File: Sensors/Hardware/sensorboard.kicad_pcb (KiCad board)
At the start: 4 copper layers, 100 x 50 mm, 260 parts, among them J1 RBUS, J10 1053131104, J11 1053131104, J12 1053131104, J13 1053131104, J14 1053131104, J15 USB_C_Receptacle_USB2.0, J16 Micro_SD_Card_Det, J2 Conn_Coaxial, J3 1053131104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

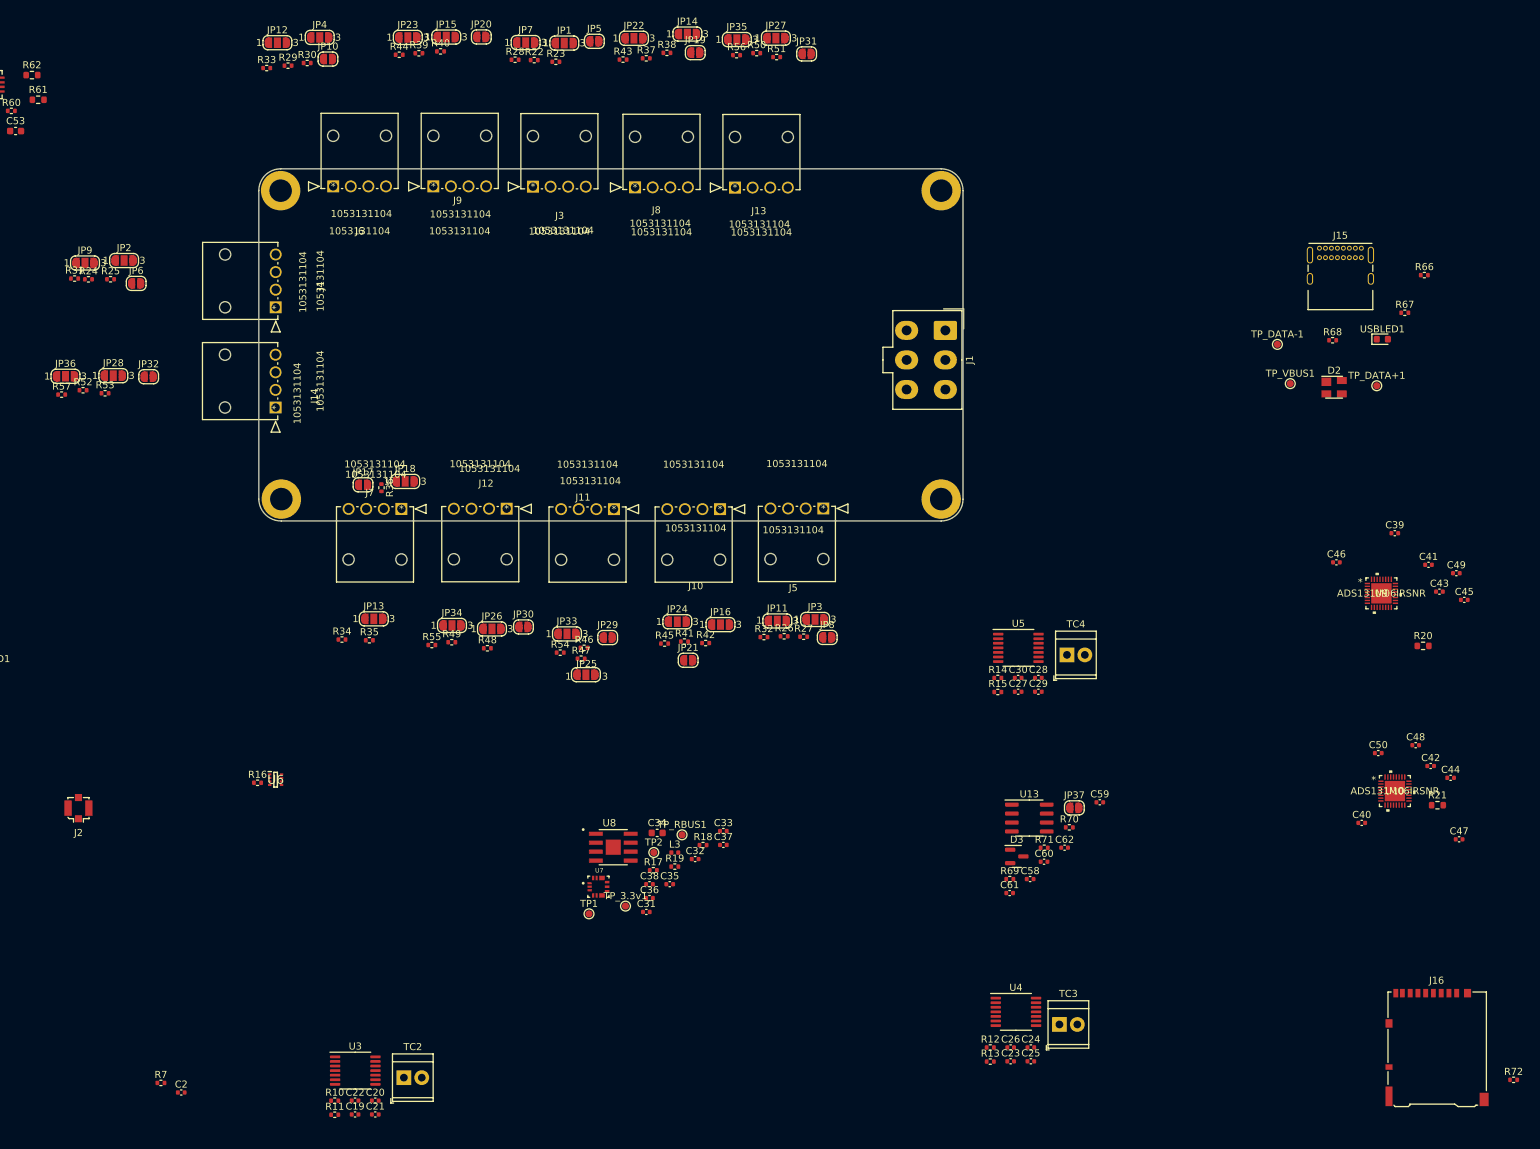
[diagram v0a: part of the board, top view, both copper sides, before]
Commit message: nanofit placements
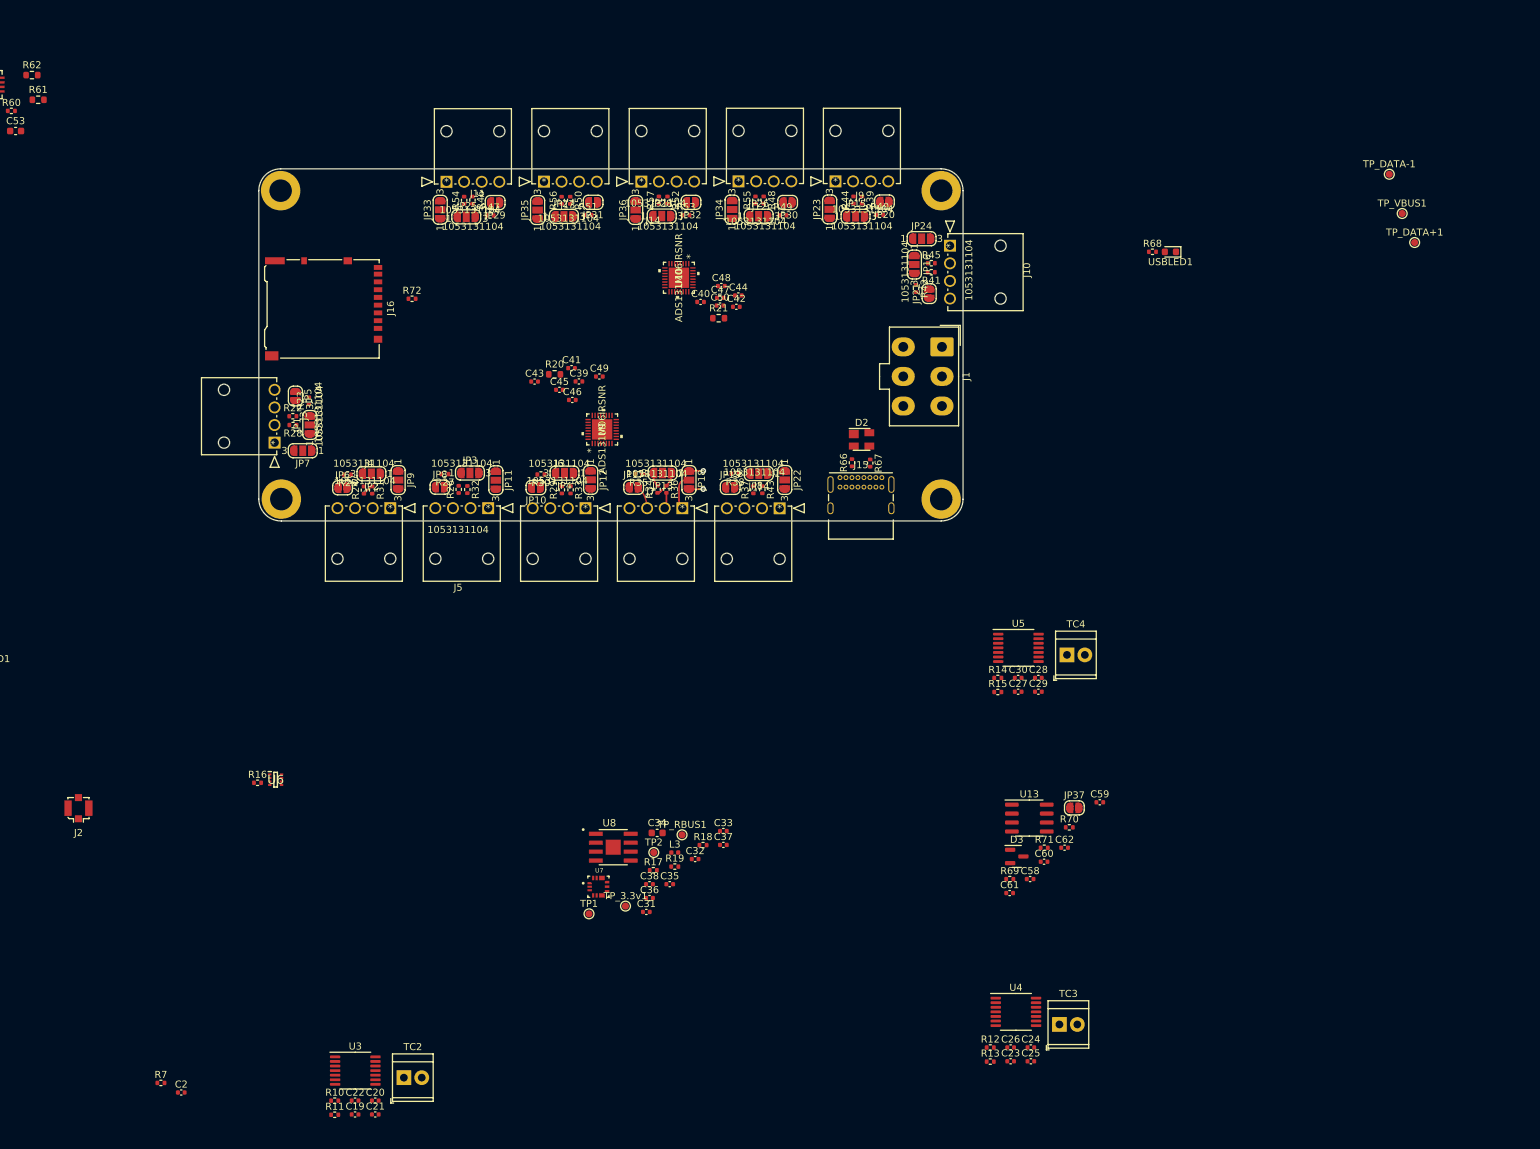
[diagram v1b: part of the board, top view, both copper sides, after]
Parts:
- moved R72 191.8 mm to (121.8, 48.5)
- moved J16 189.7 mm to (109.2, 49.9), turned to -90 degrees
- moved C45 131.9 mm to (142.7, 61.4)
- moved C43 131.9 mm to (139.2, 60.2)
- moved C47 130.1 mm to (165.5, 48.3)
- moved R20 129.2 mm to (142.0, 59.2)
- moved U10 125.1 mm to (159.7, 45.5), turned to -90 degrees
- moved C41 124.9 mm to (144.4, 58.3)
- moved C49 124.9 mm to (148.4, 59.5)
- moved R21 123.3 mm to (165.3, 51.2)
- moved C44 122.2 mm to (168.1, 48.0)
- moved C40 119.5 mm to (162.7, 48.9)
- moved C42 118.2 mm to (167.8, 49.6)
- moved C48 118.2 mm to (165.7, 46.6)
- moved C39 117.8 mm to (145.5, 60.2)
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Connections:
- 12VLED1 pad 1: +3V3 -> GND
- 3V3LED1 pad 1: +3V3 -> GND
- BOOTJUMPER1 pad 2: +3V3 -> GND
- C1 pad 2: +3V3 -> GND
- C10 pad 2: +3V3 -> GND
- C12 pad 2: +3V3 -> GND
- C13 pad 2: +3V3 -> GND
- C14 pad 2: +3V3 -> GND
- C15 pad 1: +3V3 -> GND
- C17 pad 2: +3V3 -> GND
- C18 pad 1: +3V3 -> GND
- C19 pad 1: +3V3 -> GND
- C2 pad 2: +3V3 -> GND
- C21 pad 2: +3V3 -> GND
- C22 pad 1: +3V3 -> GND
- C23 pad 1: +3V3 -> GND
- C25 pad 2: +3V3 -> GND
- C26 pad 1: +3V3 -> GND
- C27 pad 1: +3V3 -> GND
- C29 pad 2: +3V3 -> GND
- C3 pad 2: +3V3 -> GND
- C30 pad 1: +3V3 -> GND
- C31 pad 2: +3V3 -> GND
- C32 pad 2: +3V3 -> GND
- C33 pad 2: +3V3 -> GND
- C34 pad 2: +3V3 -> GND
- C35 pad 2: +3V3 -> GND
- C36 pad 2: +3V3 -> GND
- C37 pad 1: +3V3 -> GND
- C38 pad 1: +3V3 -> GND
- C39 pad 1: +3V3 -> GND
- C4 pad 2: +3V3 -> GND
- C40 pad 1: +3V3 -> GND
- C41 pad 2: +3V3 -> GND
- C42 pad 2: +3V3 -> GND
- C43 pad 2: +3V3 -> GND
- C44 pad 2: +3V3 -> GND
- C45 pad 2: +3V3 -> GND
- C46 pad 2: +3V3 -> GND
- C47 pad 2: +3V3 -> GND
- C48 pad 2: +3V3 -> GND
- C49 pad 2: +3V3 -> GND
- C5 pad 2: +3V3 -> GND
- C50 pad 2: +3V3 -> GND
- C51 pad 2: +3V3 -> GND
- C52 pad 2: +3V3 -> GND
- C53 pad 2: +3V3 -> GND
- C54 pad 2: +3V3 -> GND
- C56 pad 2: +3V3 -> GND
- C57 pad 2: +3V3 -> GND
- C58 pad 2: +3V3 -> GND
- C59 pad 2: +3V3 -> GND
- C6 pad 2: +3V3 -> GND
- C60 pad 2: +3V3 -> GND
- C61 pad 1: +3V3 -> GND
- C62 pad 1: +3V3 -> GND
- C7 pad 2: +3V3 -> GND
- C8 pad 2: +3V3 -> GND
- C9 pad 2: +3V3 -> GND
- D2 pad 1: +3V3 -> GND
- D3 pad 3: +3V3 -> GND
- ENJUMPER1 pad 2: +3V3 -> GND
- H1 pad 1: +3V3 -> GND
- H2 pad 1: +3V3 -> GND
- H3 pad 1: +3V3 -> GND
- H4 pad 1: +3V3 -> GND
- J1 pad 1: +3V3 -> GND
- J1 pad 2: +3V3 -> GND
- J10 pad 4: +3V3 -> GND
- J11 pad 4: +3V3 -> GND
- J12 pad 4: +3V3 -> GND
- J13 pad 4: +3V3 -> GND
- J14 pad 4: +3V3 -> GND
- J15 pad A1: +3V3 -> GND
- J15 pad A12: +3V3 -> GND
- J15 pad B1: +3V3 -> GND
- J15 pad B12: +3V3 -> GND
- J15 pad S1: +3V3 -> GND
- J16 pad 11: +3V3 -> GND
- J16 pad 6: +3V3 -> GND
- J16 pad 9: +3V3 -> GND
- J2 pad 2: +3V3 -> GND
- J3 pad 4: +3V3 -> GND
- J4 pad 4: +3V3 -> GND
- J5 pad 4: +3V3 -> GND
- J6 pad 4: +3V3 -> GND
- J7 pad 4: +3V3 -> GND
- J8 pad 4: +3V3 -> GND
- J9 pad 4: +3V3 -> GND
- JP10 pad 1: +3V3 -> GND
- JP17 pad 1: +3V3 -> GND
- JP19 pad 1: +3V3 -> GND
- JP20 pad 1: +3V3 -> GND
- JP21 pad 1: +3V3 -> GND
- JP29 pad 1: +3V3 -> GND
- JP30 pad 1: +3V3 -> GND
- JP31 pad 1: +3V3 -> GND
- JP32 pad 1: +3V3 -> GND
- JP5 pad 1: +3V3 -> GND
- JP6 pad 1: +3V3 -> GND
- JP8 pad 1: +3V3 -> GND
- R17 pad 2: +3V3 -> GND
- R19 pad 2: +3V3 -> GND
- R23 pad 2: +3V3 -> GND
- R25 pad 2: +3V3 -> GND
- R27 pad 2: +3V3 -> GND
- R30 pad 2: +3V3 -> GND
- R35 pad 2: +3V3 -> GND
- R38 pad 2: +3V3 -> GND
- R4 pad 1: +3V3 -> GND
- R40 pad 2: +3V3 -> GND
- R42 pad 2: +3V3 -> GND
- R47 pad 2: +3V3 -> GND
- R49 pad 2: +3V3 -> GND
- R51 pad 2: +3V3 -> GND
- R53 pad 2: +3V3 -> GND
- R59 pad 2: +3V3 -> GND
- R60 pad 2: +3V3 -> GND
- R64 pad 2: +3V3 -> GND
- R66 pad 2: +3V3 -> GND
- R67 pad 1: +3V3 -> GND
- R69 pad 2: +3V3 -> GND
- U1 pad 57: +3V3 -> GND
- U10 pad 13: +3V3 -> GND
- U10 pad 22: +3V3 -> GND
- U10 pad 28: +3V3 -> GND
- U10 pad 33: +3V3 -> GND
- U11 pad 10: +3V3 -> GND
- U11 pad 13: +3V3 -> GND
- U11 pad 17: +3V3 -> GND
- U11 pad 5: +3V3 -> GND
- U11 pad 6: +3V3 -> GND
- U11 pad 7: +3V3 -> GND
- U12 pad 2: +3V3 -> GND
- U12 pad 3: +3V3 -> GND
- U12 pad 9: +3V3 -> GND
- U13 pad 2: +3V3 -> GND
- U2 pad 1: +3V3 -> GND
- U2 pad 14: +3V3 -> GND
- U3 pad 1: +3V3 -> GND
- U3 pad 14: +3V3 -> GND
- U4 pad 1: +3V3 -> GND
- U4 pad 14: +3V3 -> GND
- U5 pad 1: +3V3 -> GND
- U5 pad 14: +3V3 -> GND
- U6 pad 1: +3V3 -> GND
- U6 pad 4: +3V3 -> GND
- U6 pad 5: +3V3 -> GND
- U7 pad 4: +3V3 -> GND
- U7 pad 9: +3V3 -> GND
- U8 pad 8: +3V3 -> GND
- U8 pad 9: +3V3 -> GND
- U9 pad 13: +3V3 -> GND
- U9 pad 22: +3V3 -> GND
- U9 pad 28: +3V3 -> GND
- U9 pad 33: +3V3 -> GND
- USBLED1 pad 1: +3V3 -> GND
- Y1 pad 2: +3V3 -> GND
- Y1 pad 4: +3V3 -> GND
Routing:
- net Net-(J7-Pad1): track 0.00 -> 5.10 mm
- net Net-(JP13-Pad1): track 0.00 -> 3.63 mm
- net Net-(JP13-Pad3): track 0.00 -> 3.57 mm
- net /analogueSPI/AIN4N: track 0.00 -> 3.29 mm
- net Net-(J7-Pad2): track 0.00 -> 2.69 mm
- net +3V3: track 0.00 -> 2.04 mm, vias 0 -> 1
- net +5V: track 0.00 -> 2.03 mm, vias 0 -> 1
- net Net-(JP2-Pad1): track 0.00 -> 1.58 mm

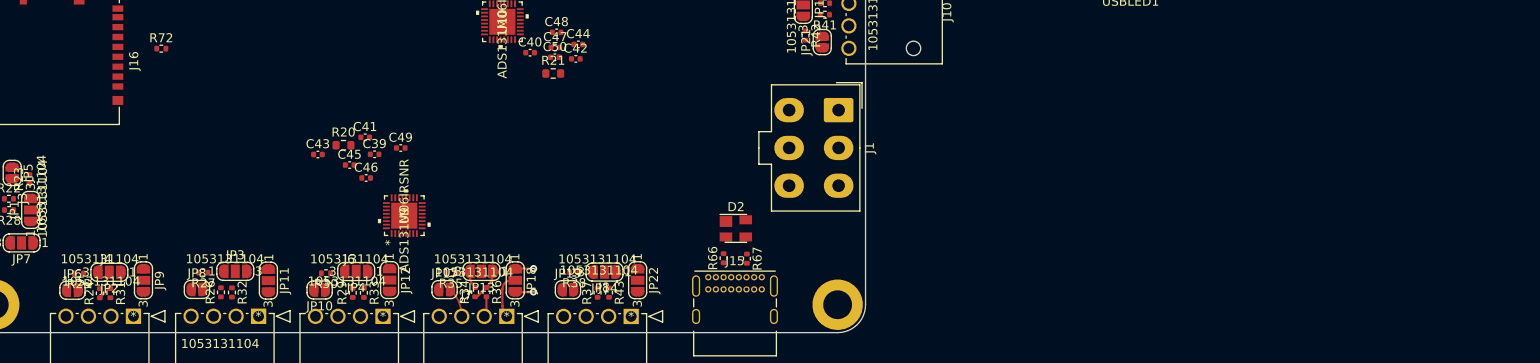
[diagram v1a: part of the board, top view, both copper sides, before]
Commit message: added low pass filters for ADC inputs
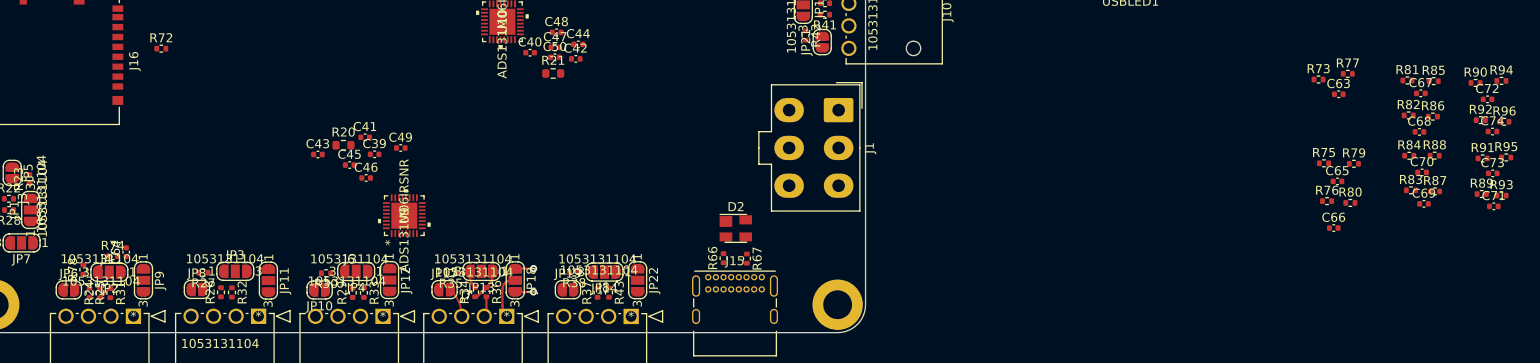
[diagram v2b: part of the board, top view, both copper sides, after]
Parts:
- added C63: 10nF, Capacitor_SMD:C_0402_1005Metric, F.Cu at (252.6, 53.5)
- added C64: 10nF, Capacitor_SMD:C_0402_1005Metric, F.Cu at (117.9, 71.1)
- added C65: 10nF, Capacitor_SMD:C_0402_1005Metric, F.Cu at (252.4, 63.2)
- added C66: 10nF, Capacitor_SMD:C_0402_1005Metric, F.Cu at (252.0, 68.4)
- added C67: 10nF, Capacitor_SMD:C_0402_1005Metric, F.Cu at (261.7, 53.4)
- added C68: 10nF, Capacitor_SMD:C_0402_1005Metric, F.Cu at (261.5, 57.7)
- added C69: 10nF, Capacitor_SMD:C_0402_1005Metric, F.Cu at (262.0, 65.7)
- added C70: 10nF, Capacitor_SMD:C_0402_1005Metric, F.Cu at (261.8, 62.2)
- added C71: 10nF, Capacitor_SMD:C_0402_1005Metric, F.Cu at (269.8, 66.0)
- added C72: 10nF, Capacitor_SMD:C_0402_1005Metric, F.Cu at (269.1, 54.1)
- added C73: 10nF, Capacitor_SMD:C_0402_1005Metric, F.Cu at (269.7, 62.3)
- added C74: 10nF, Capacitor_SMD:C_0402_1005Metric, F.Cu at (269.6, 57.7)
- added R73: 1k, Resistor_SMD:R_0402_1005Metric, F.Cu at (250.3, 51.9)
- added R74: 1k, Resistor_SMD:R_0402_1005Metric, F.Cu at (116.4, 71.5)
- added R75: 1k, Resistor_SMD:R_0402_1005Metric, F.Cu at (250.9, 61.2)
- added R76: 1k, Resistor_SMD:R_0402_1005Metric, F.Cu at (251.3, 65.4)
- added R77: 1k, Resistor_SMD:R_0402_1005Metric, F.Cu at (253.6, 51.2)
- added R78: 1k, Resistor_SMD:R_0402_1005Metric, F.Cu at (113.1, 73.0)
- added R79: 1k, Resistor_SMD:R_0402_1005Metric, F.Cu at (254.3, 61.2)
- added R80: 1k, Resistor_SMD:R_0402_1005Metric, F.Cu at (253.9, 65.6)
- added R81: 1k, Resistor_SMD:R_0402_1005Metric, F.Cu at (260.2, 52.0)
- added R82: 1k, Resistor_SMD:R_0402_1005Metric, F.Cu at (260.3, 55.9)
- added R83: 1k, Resistor_SMD:R_0402_1005Metric, F.Cu at (260.6, 64.2)
- added R84: 1k, Resistor_SMD:R_0402_1005Metric, F.Cu at (260.4, 60.4)
- added R85: 1k, Resistor_SMD:R_0402_1005Metric, F.Cu at (263.1, 52.1)
- added R86: 1k, Resistor_SMD:R_0402_1005Metric, F.Cu at (263.0, 56.0)
- added R87: 1k, Resistor_SMD:R_0402_1005Metric, F.Cu at (263.3, 64.3)
- added R88: 1k, Resistor_SMD:R_0402_1005Metric, F.Cu at (263.2, 60.3)
- added R89: 1k, Resistor_SMD:R_0402_1005Metric, F.Cu at (268.5, 64.6)
- added R90: 1k, Resistor_SMD:R_0402_1005Metric, F.Cu at (267.8, 52.3)
- added R91: 1k, Resistor_SMD:R_0402_1005Metric, F.Cu at (268.6, 60.6)
- added R92: 1k, Resistor_SMD:R_0402_1005Metric, F.Cu at (268.4, 56.4)
- added R93: 1k, Resistor_SMD:R_0402_1005Metric, F.Cu at (270.7, 64.8)
- added R94: 1k, Resistor_SMD:R_0402_1005Metric, F.Cu at (270.6, 52.0)
- added R95: 1k, Resistor_SMD:R_0402_1005Metric, F.Cu at (271.2, 60.5)
- added R96: 1k, Resistor_SMD:R_0402_1005Metric, F.Cu at (271.0, 56.6)
- moved R25 2.47 mm to (113.8, 75.6), turned to -90 degrees
- moved JP6 0.40 mm to (111.5, 75.2)
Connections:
- J10 pad 3: /analogueSPI/AIN6N -> Net-(J10-Pad3)
- J11 pad 3: /analogueSPI/AIN11N -> Net-(J11-Pad3)
- J12 pad 3: /analogueSPI/AIN8N -> Net-(J12-Pad3)
- J13 pad 3: /analogueSPI/AIN10N -> Net-(J13-Pad3)
- J14 pad 3: /analogueSPI/AIN9N -> Net-(J14-Pad3)
- J3 pad 3: /analogueSPI/AIN0N -> Net-(J3-Pad3)
- J4 pad 3: /analogueSPI/AIN1N -> Net-(J4-Pad3)
- J5 pad 3: /analogueSPI/AIN2N -> Net-(J5-Pad3)
- J6 pad 3: /analogueSPI/AIN3N -> Net-(J6-Pad3)
- J7 pad 3: /analogueSPI/AIN4N -> Net-(J7-Pad3)
- J8 pad 3: /analogueSPI/AIN5N -> Net-(J8-Pad3)
- J9 pad 3: /analogueSPI/AIN7N -> Net-(J9-Pad3)
- JP1 pad 2: /analogueSPI/AIN0P -> Net-(JP1-Pad2)
- JP10 pad 2: /analogueSPI/AIN3N -> Net-(J6-Pad3)
- JP13 pad 2: /analogueSPI/AIN4P -> Net-(JP13-Pad2)
- JP14 pad 2: /analogueSPI/AIN5P -> Net-(JP14-Pad2)
- JP15 pad 2: /analogueSPI/AIN7P -> Net-(JP15-Pad2)
- JP16 pad 2: /analogueSPI/AIN6P -> Net-(JP16-Pad2)
- JP17 pad 2: /analogueSPI/AIN4N -> Net-(J7-Pad3)
- JP19 pad 2: /analogueSPI/AIN5N -> Net-(J8-Pad3)
- JP2 pad 2: /analogueSPI/AIN1P -> Net-(JP2-Pad2)
- JP20 pad 2: /analogueSPI/AIN7N -> Net-(J9-Pad3)
- JP21 pad 2: /analogueSPI/AIN6N -> Net-(J10-Pad3)
- JP25 pad 2: /analogueSPI/AIN11P -> Net-(JP25-Pad2)
- JP26 pad 2: /analogueSPI/AIN8P -> Net-(JP26-Pad2)
- JP27 pad 2: /analogueSPI/AIN10P -> Net-(JP27-Pad2)
- JP28 pad 2: /analogueSPI/AIN9P -> Net-(JP28-Pad2)
- JP29 pad 2: /analogueSPI/AIN11N -> Net-(J11-Pad3)
- JP3 pad 2: /analogueSPI/AIN2P -> Net-(JP3-Pad2)
- JP30 pad 2: /analogueSPI/AIN8N -> Net-(J12-Pad3)
- JP31 pad 2: /analogueSPI/AIN10N -> Net-(J13-Pad3)
- JP32 pad 2: /analogueSPI/AIN9N -> Net-(J14-Pad3)
- JP4 pad 2: /analogueSPI/AIN3P -> Net-(JP4-Pad2)
- JP5 pad 2: /analogueSPI/AIN0N -> Net-(J3-Pad3)
- JP6 pad 2: /analogueSPI/AIN1N -> Net-(J4-Pad3)
- JP8 pad 2: /analogueSPI/AIN2N -> Net-(J5-Pad3)
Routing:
- net Net-(J7-Pad3): track 0.00 -> 3.29 mm
- net /analogueSPI/AIN4N: track 3.29 -> 0.00 mm

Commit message: update before power layout
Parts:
- added C21: 10uF, Capacitor_SMD:C_0603_1608Metric, F.Cu at (123.4, 134.9)
- added L3: 1uH, Inductor_SMD:L_0805_2012Metric, F.Cu at (125.9, 137.3)
- moved C65 123.1 mm to (129.5, 69.2)
- moved R75 123.1 mm to (128.0, 67.2)
- moved R79 123.1 mm to (131.3, 67.2)
- moved C33 43.1 mm to (123.6, 132.2), turned to 90 degrees
- moved C32 39.2 mm to (123.4, 134.9), turned to -90 degrees
- moved C37 38.0 mm to (130.1, 138.3)
- moved L3 34.7 mm to (125.9, 137.3)
- moved R18 33.5 mm to (131.9, 138.4)
- moved C31 32.5 mm to (122.7, 132.2), turned to 90 degrees
- moved R17 30.3 mm to (125.7, 131.3), turned to 180 degrees
- moved C34 30.0 mm to (128.4, 134.8), turned to -90 degrees
- moved R16 28.8 mm to (121.8, 135.7), turned to 90 degrees
- moved R19 26.9 mm to (133.8, 138.4)
- moved C38 26.6 mm to (130.1, 139.3)
- moved C35 25.3 mm to (133.1, 130.0)
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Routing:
- net /Power/BBOUT: track 0.00 -> 12.3 mm
- net GND: track 0.00 -> 6.73 mm, vias 0 -> 8
- net /analogueSPI/AIN1N: track 0.00 -> 5.52 mm
- net Net-(J4-Pad3): track 0.00 -> 5.44 mm
- net VBUS: track 0.00 -> 5.27 mm, vias 0 -> 2
- net Net-(J4-Pad1): track 0.00 -> 4.86 mm
- net /Power/BBIN: track 0.00 -> 3.68 mm
- net Net-(JP2-Pad3): track 0.00 -> 3.65 mm
- net /Power/FBIn: track 0.00 -> 2.61 mm
- net Net-(JP2-Pad1): track 1.58 -> 3.80 mm
- net Net-(J4-Pad2): track 0.00 -> 2.08 mm
- net Net-(JP2-Pad2): track 0.00 -> 1.82 mm
- net +3V3: track 2.04 -> 3.65 mm, vias 1 -> 2
- net /Power/BIAS: track 0.00 -> 1.42 mm
- net /Power/SEL: track 0.00 -> 1.01 mm
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- added copper zone on F.Cu, net +3V3
- added copper zone on F.Cu, net /Power/BBIN
- added copper zone on F.Cu, net /Power/BBOUT
- added copper zone on B.Cu, net /Power/LX1
- added copper zone on F.Cu, net /Power/LX1
- added copper zone on B.Cu, net /Power/LX2
- added copper zone on F.Cu, net /Power/LX2
- added copper zone on F.Cu, net GND

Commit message: power layout done
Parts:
- removed the C21 at (123.4, 134.9)
- removed the L3 at (125.9, 137.3)
- C32: footprint Capacitor_SMD:C_0402_1005Metric -> Capacitor_SMD:C_0603_1608Metric
- L3: footprint Inductor_SMD:L_0402_1005Metric -> Inductor_SMD:L_0805_2012Metric
